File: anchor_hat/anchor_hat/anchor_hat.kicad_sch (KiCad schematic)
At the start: 25 parts, among them J1 GPIO, J2 Motor 1, J3 Motor 2, J4 24v in barrel jack, J5 24v out slip ring, J6 5v out fan, J7 5v out fan right angle, U2 MCP2515-xST, U3 SN65HVD230, U4 TPS54302, Y1 12M

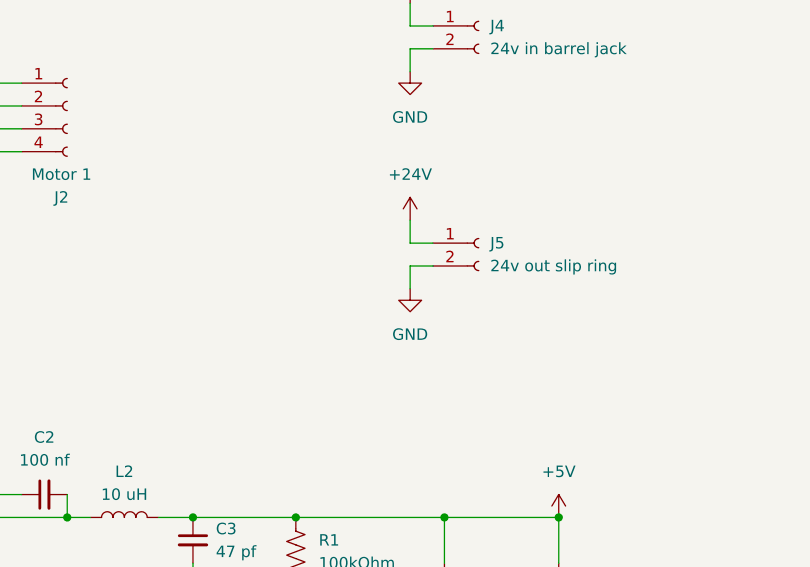
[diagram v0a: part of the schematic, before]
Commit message: swap terminals on slip ring plug so ground is the lower pin
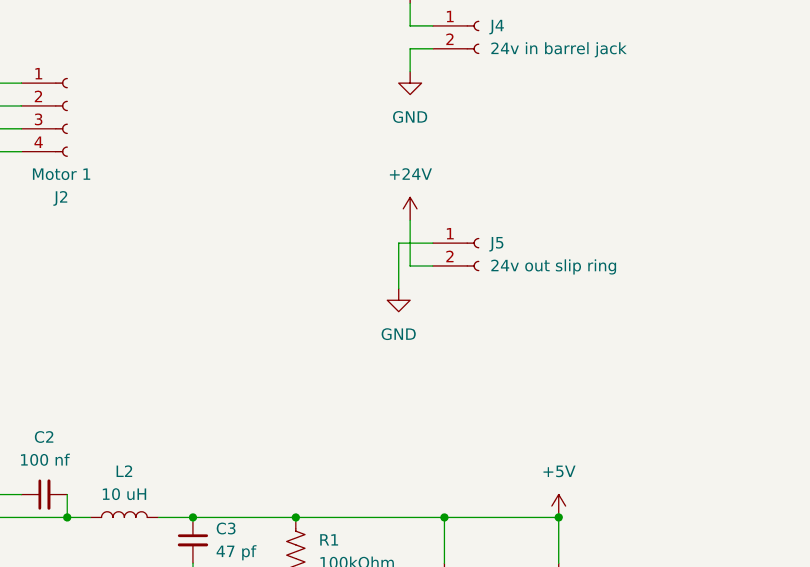
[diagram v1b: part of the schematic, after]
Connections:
- net +24V: now also J5.2 (Pin_2); no longer J5.1 (Pin_1)
- net GND: now also J5.1 (Pin_1); no longer J5.2 (Pin_2)
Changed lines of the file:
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@@
 	(wire
 		(pts
+			(xy 238.76 90.17) (xy 238.76 85.09)
+		)
+		(stroke
+			(width 0)
+			(type default)
+		)
+	)
+	(wire
+		(pts
 			(xy 190.5 35.56) (xy 190.5 40.64)
 		)
@@
 	(wire
 		(pts
-			(xy 240.03 85.09) (xy 240.03 82.55)
+			(xy 240.03 82.55) (xy 240.03 87.63)
 		)
 		(stroke
@@
 	(wire
 		(pts
-			(xy 240.03 87.63) (xy 242.57 87.63)
-		)
-		(stroke
-			(width 0)
-			(type default)
-		)
-	)
-	(wire
-		(pts
 			(xy 256.54 130.81) (xy 256.54 125.73)
 		)
@@
 	(wire
 		(pts
-			(xy 240.03 90.17) (xy 240.03 87.63)
-		)
-		(stroke
-			(width 0)
-			(type default)
-		)
-	)
-	(wire
-		(pts
 			(xy 125.73 54.61) (xy 130.81 54.61)
 		)
@@
 	(wire
 		(pts
+			(xy 240.03 87.63) (xy 242.57 87.63)
+		)
+		(stroke
+			(width 0)
+			(type default)
+		)
+	)
+	(wire
+		(pts
 			(xy 31.75 33.02) (xy 60.96 33.02)
 		)
@@
 	(wire
 		(pts
+			(xy 238.76 85.09) (xy 242.57 85.09)
+		)
+		(stroke
+			(width 0)
+			(type default)
+		)
+	)
+	(wire
+		(pts
 			(xy 76.2 24.13) (xy 76.2 27.94)
 		)
@@
 	(wire
 		(pts
-			(xy 242.57 85.09) (xy 240.03 85.09)
-		)
-		(stroke
-			(width 0)
-			(type default)
-		)
-	)
-	(wire
-		(pts
 			(xy 160.02 113.03) (xy 173.99 113.03)
 		)
@@
 		(lib_name "GND_4")
 		(lib_id "power:GND")
-		(at 240.03 90.17 0)
+		(at 238.76 90.17 0)
 		(unit 1)
 		(exclude_from_sim no)
@@
 		(fields_autoplaced yes)
 		(property "Reference" "#PWR020"
-			(at 240.03 96.52 0)
+			(at 238.76 96.52 0)
 			(effects
 				(font
@@
 		)
 		(property "Value" "GND"
-			(at 240.03 95.25 0)
+			(at 238.76 95.25 0)
 			(effects
 				(font
@@
 		)
 		(property "Footprint" ""
-			(at 240.03 90.17 0)
+			(at 238.76 90.17 0)
 			(effects
 				(font
@@
 		)
 		(property "Datasheet" ""
-			(at 240.03 90.17 0)
+			(at 238.76 90.17 0)
 			(effects
 				(font
@@
 		)
 		(property "Description" "Power symbol creates a global label with name \"GND\" , ground"
-			(at 240.03 90.17 0)
+			(at 238.76 90.17 0)
 			(effects
 				(font

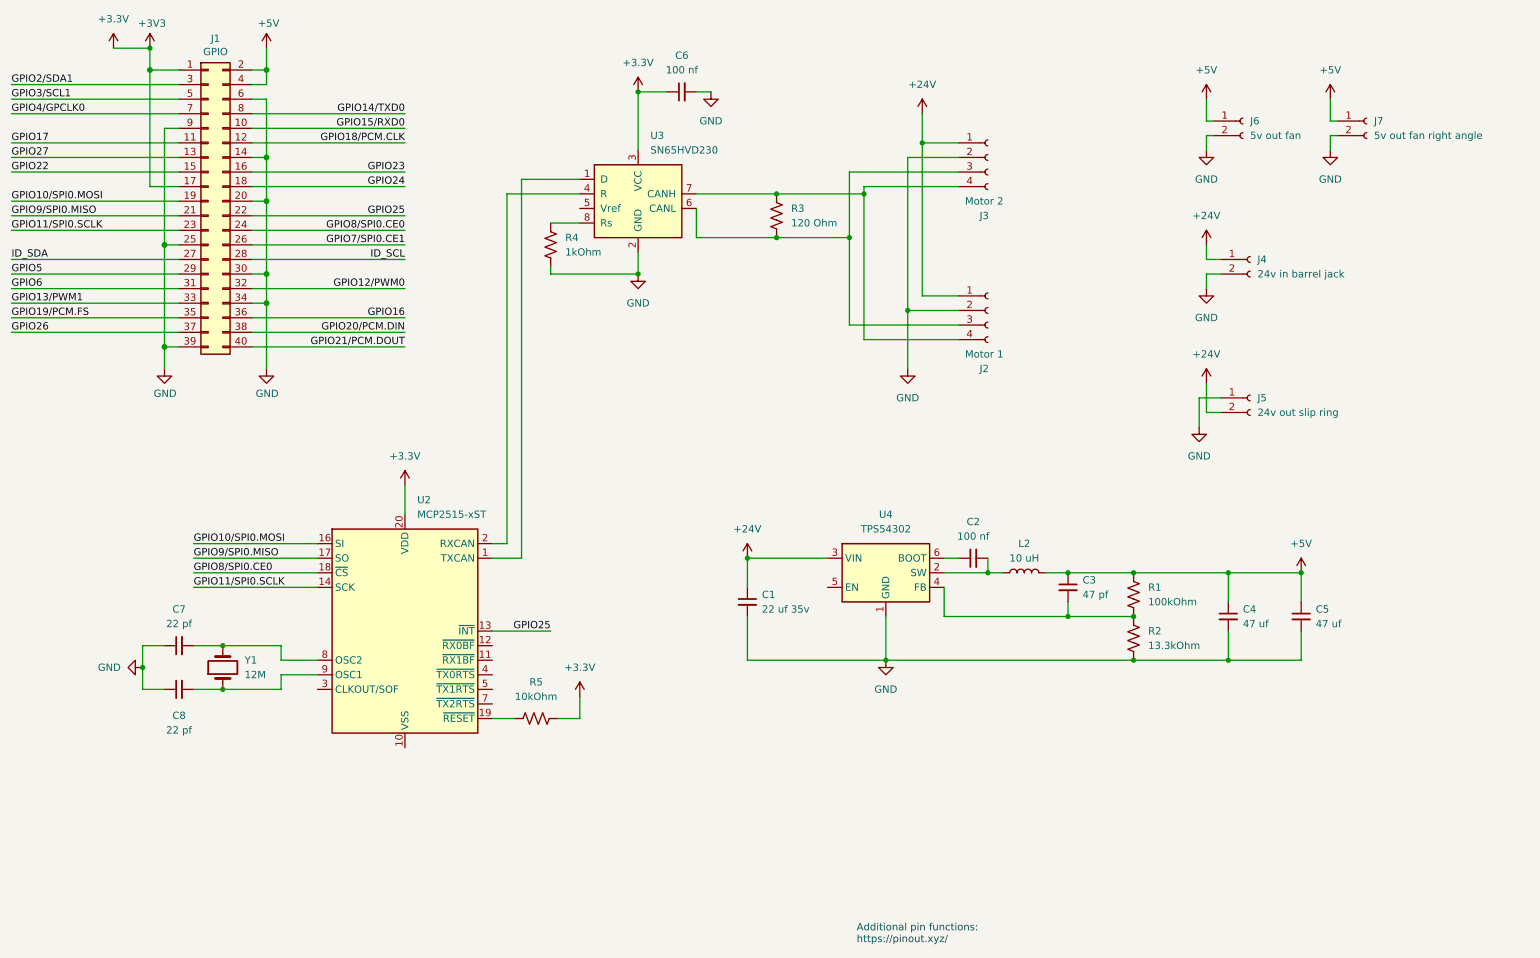
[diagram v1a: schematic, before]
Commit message: add elec cap to 24v rail on anchors
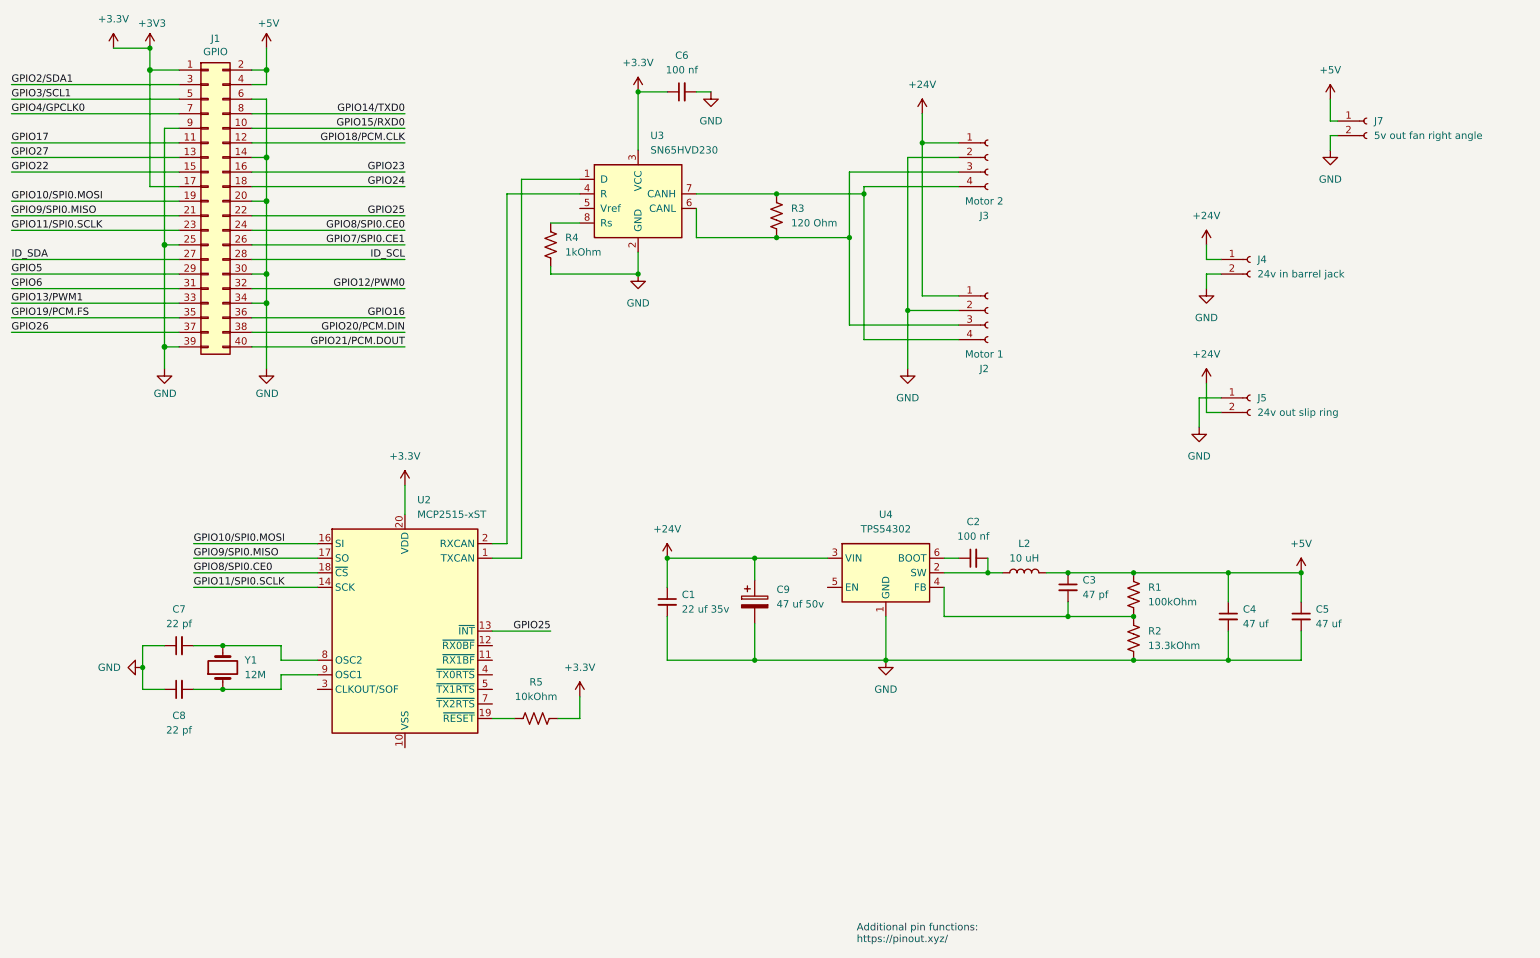
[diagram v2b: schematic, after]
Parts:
- removed J6: 5v out fan, Connector_JST:JST_PH_B2B-PH-K_1x02_P2.00mm_Vertical, symbol Connector:Conn_01x02_Socket
- added C9: 47 uf 50v, Capacitor_SMD:CP_Elec_6.3x7.7, symbol Device:C_Polarized
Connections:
- net +24V: now also C9.1
- net GND: now also C9.2
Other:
- moved on the sheet: C1
